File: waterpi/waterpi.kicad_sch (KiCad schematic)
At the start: 33 parts, among them J1 RPi, J10 OUT6, J11 OUT7, J14 ADC0, J15 ADC1, J16 ADC2, J17 ADC3, J18 ADC4, J19 ADC5, J20 ADC6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

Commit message: Rename garduino to waterpi
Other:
- title: garduino -> waterpi
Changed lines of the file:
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@@
 	(paper "A4")
 	(title_block
-		(title "garduino")
+		(title "waterpi")
 		(rev "v1")
 		(company "lars@ibp.de")
@@
 		)
 		(instances
-			(project "garduino"
+			(project "waterpi"
 				(path "/2a88fe87-76f2-4b3c-835b-0e8ca2d29d4a"
 					(reference "J21")
@@
 		)
 		(instances
-			(project "garduino"
+			(project "waterpi"
 				(path "/2a88fe87-76f2-4b3c-835b-0e8ca2d29d4a"
 					(reference "#PWR020")
@@
 		)
 		(instances
-			(project "garduino"
+			(project "waterpi"
 				(path "/2a88fe87-76f2-4b3c-835b-0e8ca2d29d4a"
 					(reference "#PWR016")
@@
 		)
 		(instances
-			(project "garduino"
+			(project "waterpi"
 				(path "/2a88fe87-76f2-4b3c-835b-0e8ca2d29d4a"
 					(reference "#PWR013")
@@
 		)
 		(instances
-			(project "garduino"
+			(project "waterpi"
 				(path "/2a88fe87-76f2-4b3c-835b-0e8ca2d29d4a"
 					(reference "C3")
@@
 		)
 		(instances
-			(project "garduino"
+			(project "waterpi"
 				(path "/2a88fe87-76f2-4b3c-835b-0e8ca2d29d4a"
 					(reference "#PWR07")
@@
 		)
 		(instances
-			(project "garduino"
+			(project "waterpi"
 				(path "/2a88fe87-76f2-4b3c-835b-0e8ca2d29d4a"
 					(reference "#PWR049")
@@
 		)
 		(instances
-			(project "garduino"
+			(project "waterpi"
 				(path "/2a88fe87-76f2-4b3c-835b-0e8ca2d29d4a"
 					(reference "#PWR017")
@@
 		)
 		(instances
-			(project "garduino"
+			(project "waterpi"
 				(path "/2a88fe87-76f2-4b3c-835b-0e8ca2d29d4a"
 					(reference "C4")
@@
 		)
 		(instances
-			(project "garduino"
+			(project "waterpi"
 				(path "/2a88fe87-76f2-4b3c-835b-0e8ca2d29d4a"
 					(reference "#PWR050")
@@
 		)
 		(instances
-			(project "garduino"
+			(project "waterpi"
 				(path "/2a88fe87-76f2-4b3c-835b-0e8ca2d29d4a"
 					(reference "#PWR019")

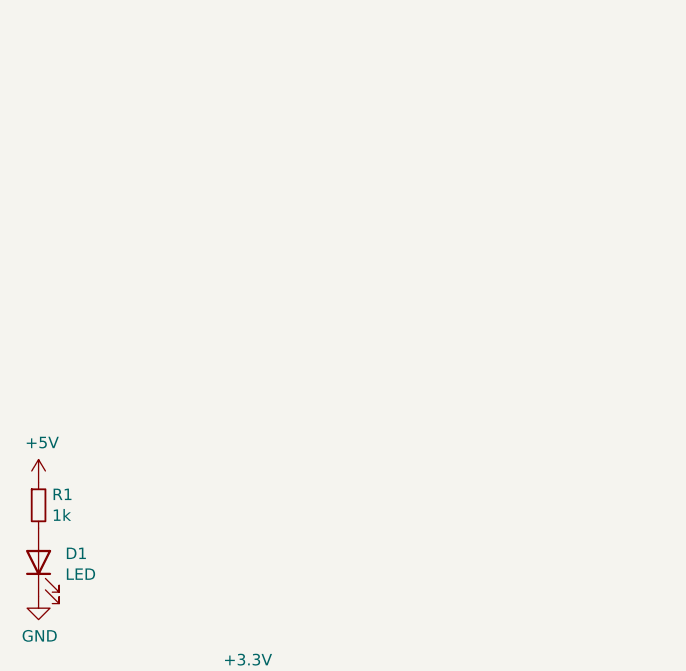
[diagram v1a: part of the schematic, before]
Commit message: Add connector for display
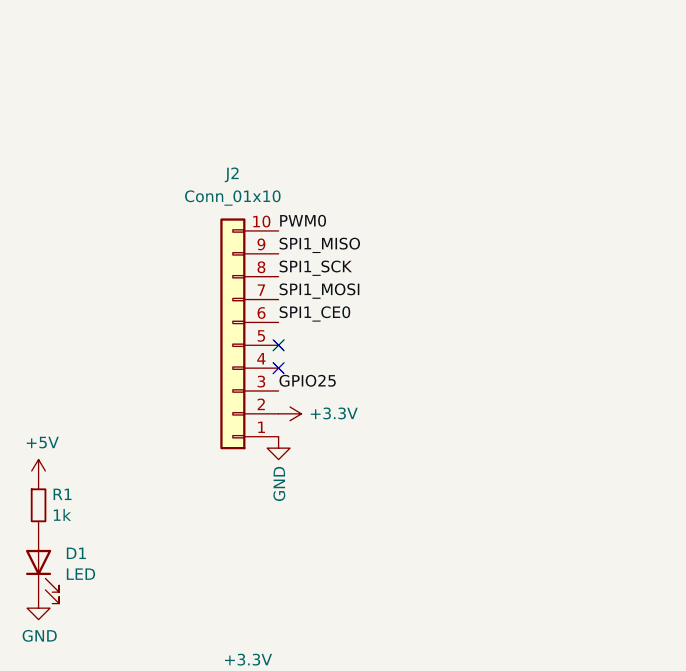
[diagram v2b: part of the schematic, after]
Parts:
- added J2: Conn_01x10, Connector_PinSocket_2.54mm:PinSocket_1x10_P2.54mm_Vertical, symbol Connector_Generic:Conn_01x10
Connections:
- net +3.3V: now also J2.2 (Pin_2)
- net GND: now also J2.1 (Pin_1)
- net GPIO25: now also J2.3 (Pin_3)
- net PWM0: now also J2.10 (Pin_10)
- net SPI1_CE0: now also J2.6 (Pin_6)
- net SPI1_MISO: now also J2.9 (Pin_9)
- net SPI1_MOSI: now also J2.7 (Pin_7)
- new net SPI1_SCK: J2.8 (Pin_8)
- no-connect marks 0 -> 2

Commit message: Remove old schematic
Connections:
- net +3.3V: no longer U1.15 (Vref)
- net +5V: now also U1.15 (Vref)
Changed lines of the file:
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@@
 	)
 	(junction
-		(at 119.38 87.63)
-		(diameter 0)
-		(color 0 0 0 0)
-	)
-	(junction
 		(at 39.37 166.37)
 		(diameter 0)
@@
 	(wire
 		(pts
-			(xy 111.76 87.63) (xy 119.38 87.63)
-		)
-		(stroke
-			(width 0)
-			(type default)
-		)
-	)
-	(wire
-		(pts
 			(xy 72.39 143.51) (xy 72.39 142.24)
 		)
@@
 					(unit 1)
 				)
+			)
+		)
+	)
+	(symbol
+		(lib_id "power:+5V")
+		(at 111.76 87.63 0)
+		(unit 1)
+		(exclude_from_sim no)
+		(in_bom yes)
+		(on_board yes)
+		(dnp no)
+		(property "Reference" "#PWR034"
+			(at 111.76 91.44 0)
+			(effects
+				(font
+					(size 1.27 1.27)
+				)
+				(hide yes)
+			)
+		)
+		(property "Value" "+5V"
+			(at 112.141 84.3788 90)
+			(effects
+				(font
+					(size 1.27 1.27)
+				)
+				(justify left)
+			)
+		)
+		(property "Footprint" ""
+			(at 111.76 87.63 0)
+			(effects
+				(font
+					(size 1.27 1.27)
+				)
+				(hide yes)
+			)
+		)
+		(property "Datasheet" ""
+			(at 111.76 87.63 0)
+			(effects
+				(font
+					(size 1.27 1.27)
+				)
+				(hide yes)
+			)
+		)
+		(property "Description" ""
+			(at 111.76 87.63 0)
+			(effects
+				(font
+					(size 1.27 1.27)
+				)
+				(hide yes)
+			)
+		)
+		(pin "1"
+		)
+		(instances
+			(project "waterpi"
+				(path "/2a88fe87-76f2-4b3c-835b-0e8ca2d29d4a"
+					(reference "#PWR034")
+					(unit 1)
+				)

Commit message: Use SOT-223
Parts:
- Q1, Q2, Q3, Q4, Q5, Q6, Q7, Q9: footprint Package_TO_SOT_SMD:TO-252-2 -> Package_TO_SOT_SMD:SOT-223-3_TabPin2
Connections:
- net +3.3V: now also J14.2 (Pin_2), J15.2 (Pin_2), J16.2 (Pin_2), J17.2 (Pin_2), J18.2 (Pin_2), J19.2 (Pin_2), J20.2 (Pin_2), J21.2 (Pin_2)
- net +5V: no longer J14.2 (Pin_2), J15.2 (Pin_2), J16.2 (Pin_2), J17.2 (Pin_2), J18.2 (Pin_2), J19.2 (Pin_2), J20.2 (Pin_2), J21.2 (Pin_2)
